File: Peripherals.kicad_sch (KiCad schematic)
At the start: 21 parts, among them J2 Conn_01x02, J5 Conn_01x03, J6 Conn_01x03, M1 Vibrator DC Motor, U1 BMI270, U12 DRV2603RUNR, U2 OPT3004DNPR, U4 LPS22DF, U5 W25Q32JVSS

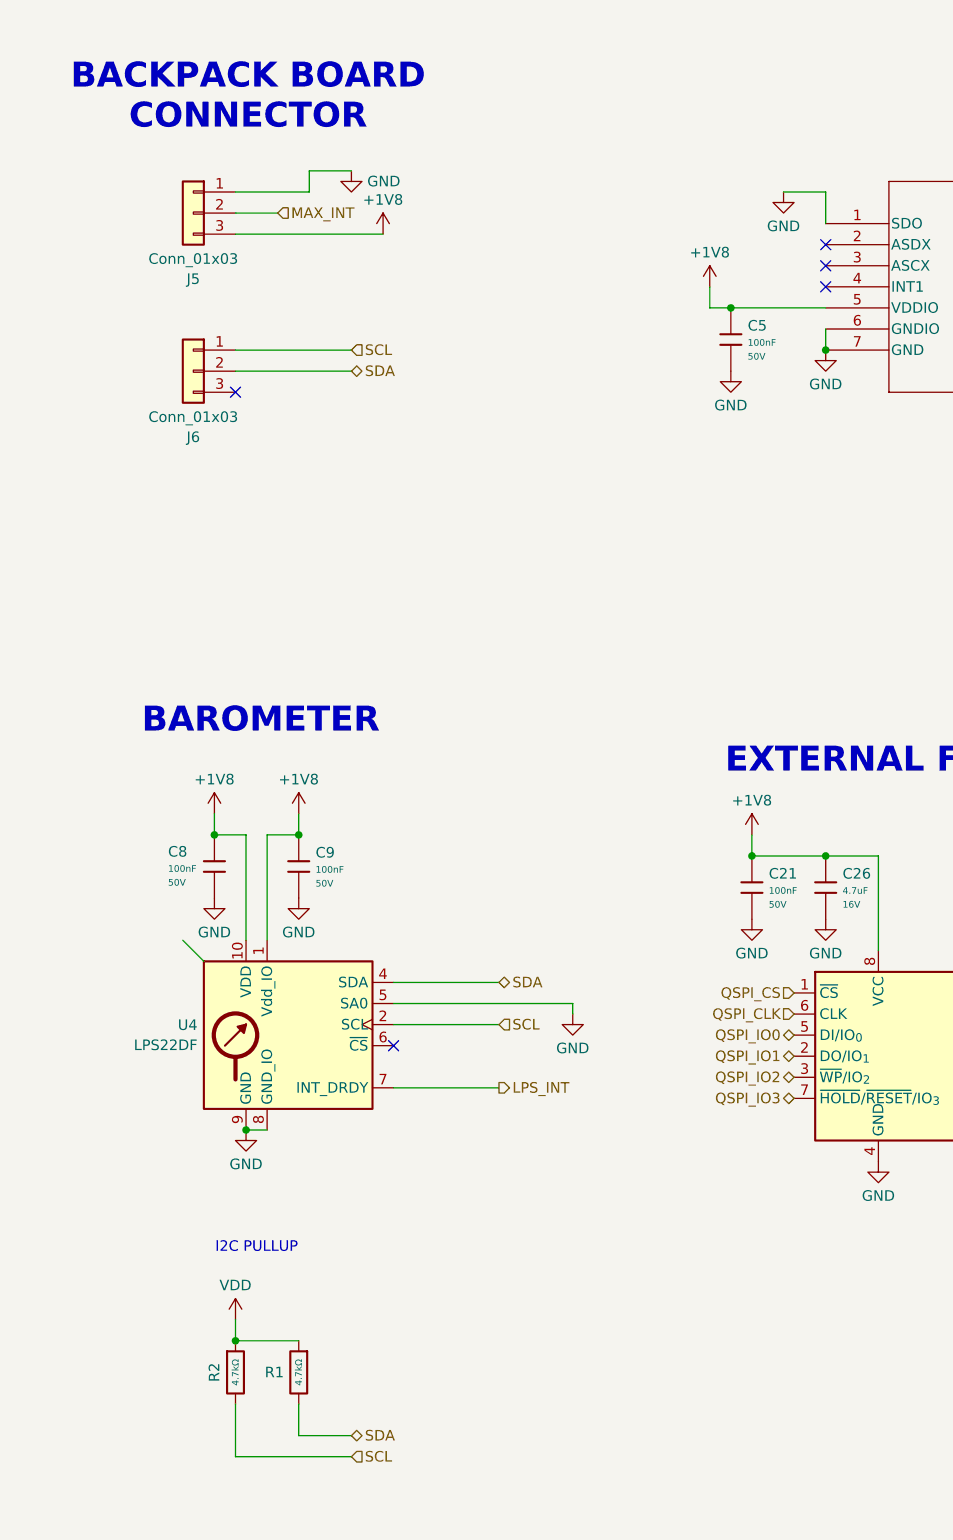
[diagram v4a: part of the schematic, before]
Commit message: Began Backpack Removal to Lower Profile
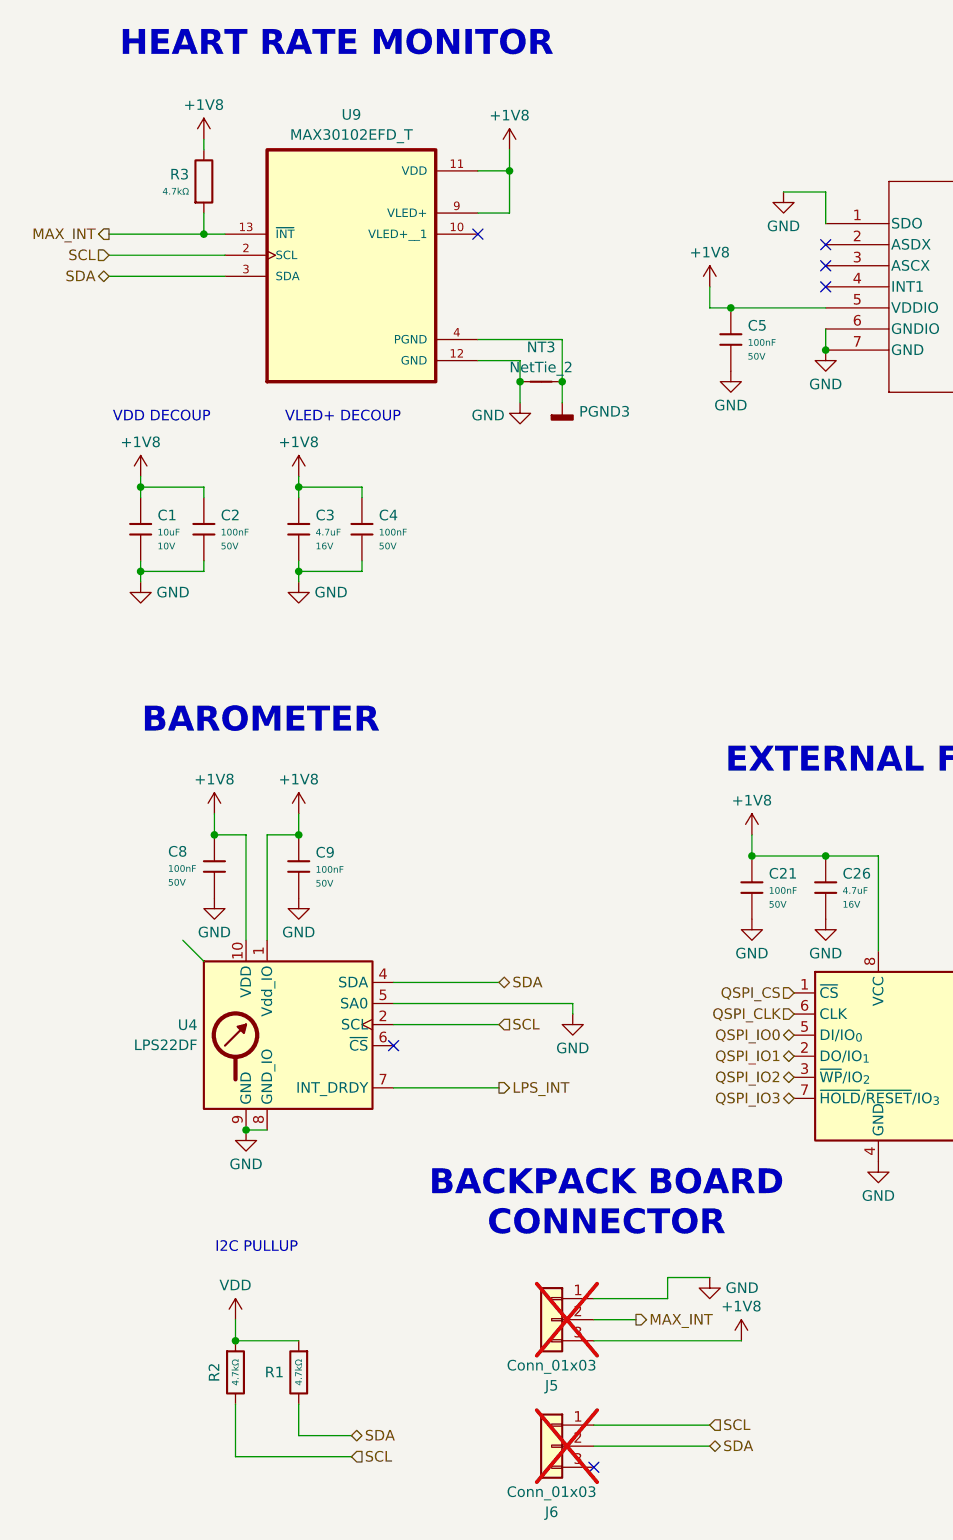
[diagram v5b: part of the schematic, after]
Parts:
- added C1: 10uF, PCM_JLCPCB:C_0603, symbol PCM_JLCPCB-Capacitors:0603,10uF
- added C2, C4: 100nF, PCM_JLCPCB:C_0603, symbol PCM_JLCPCB-Capacitors:0603,100nF
- added C3: 4.7uF, PCM_JLCPCB:C_0603, symbol PCM_JLCPCB-Capacitors:0603,4.7uF
- added NT3: NetTie_2, NetTie:NetTie-2_SMD_Pad0.5mm, symbol Device:NetTie_2
- added R3: 4.7kΩ, PCM_JLCPCB:R_0603, symbol PCM_JLCPCB-Resistors:0603,4.7kΩ
- added U9: MAX30102EFD_T, Smart_Watch:XDCR_MAX30101EFD_, symbol Smart_Watch:MAX30102EFD_T
- C21, C23, C5, C6, C7, C8, C9: Price 0.006USD -> (none)
- C26: Price 0.013USD -> (none)
- J5, J6: now not fitted
- R1, R2, R8, R9: Price 0.004USD -> (none)
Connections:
- net +1V8: now also C1.2, C2.2, C3.1, C4.1, R3.2, U9.11 (VDD), U9.9 (VLED+)
- net GND: now also C1.1, C2.1, C3.2, C4.2, NT3.1, U9.12 (GND)
- net MAX_INT: now also R3.1, U9.13 (~{INT})
- net SCL: now also U9.2 (SCL)
- net SDA: now also U9.3 (SDA)
- new net PGND3: NT3.2, U9.4 (PGND)
- no-connect marks 9 -> 10
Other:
- note added: "HEART RATE MONITOR"
- note added: "VDD DECOUP"
- note added: "VLED+ DECOUP"

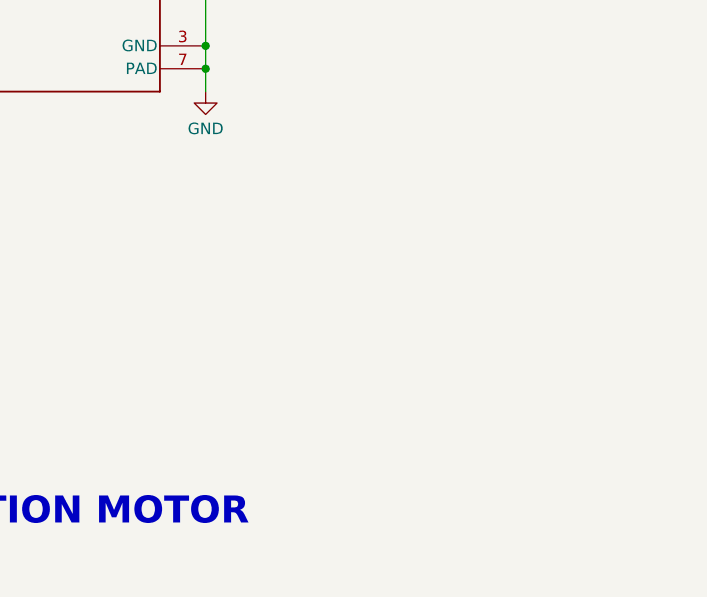
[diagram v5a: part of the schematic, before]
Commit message: Added Test Points and Changed to Top Mounted USBC
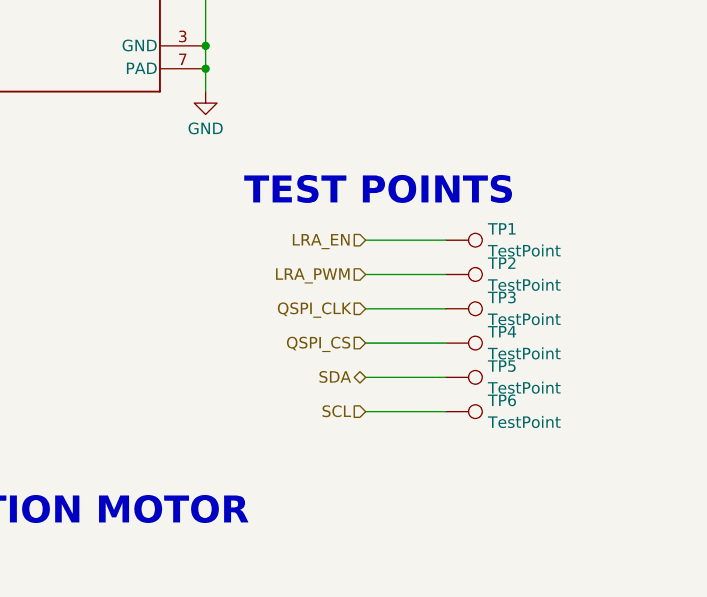
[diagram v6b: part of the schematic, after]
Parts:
- added TP1, TP2, TP3, TP4, TP5, TP6: TestPoint, TestPoint:TestPoint_Pad_1.0x1.0mm, symbol Connector:TestPoint
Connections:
- net LRA_EN: now also TP1.1
- net LRA_PWM: now also TP2.1
- net QSPI_CLK: now also TP3.1
- net QSPI_CS: now also TP4.1
- net SCL: now also TP6.1
- net SDA: now also TP5.1
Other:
- note added: "TEST POINTS"

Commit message: :)
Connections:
- net VDD is gone; now on net +1V8: R1.1, R2.1
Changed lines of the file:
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@@
 		(at 265.43 142.24)
 	)
-	(bus_entry
-		(at 36.83 127)
-		(size 2.54 2.54)
-		(stroke
-			(width 0)
-			(type default)
-		)
-	)
 	(wire
 		(pts
@@
 			)
 		)
-		(property "Value" "VDD"
-			(at 43.18 168.5869 0)
+		(property "Value" "+1V8"
+			(at 44.577 171.45 0)
 			(show_name no)
 			(do_not_autoplace no)
@@
 					(size 1.27 1.27)
 				)
+				(justify left)
 			)
 		)
